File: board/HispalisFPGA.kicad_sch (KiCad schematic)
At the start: 111 parts, among them Q1 DMG1012T, Q2 DMG1012T, Q3 DMG1012T, Q4 DMG1012T, SW1 SW_DIP_x08

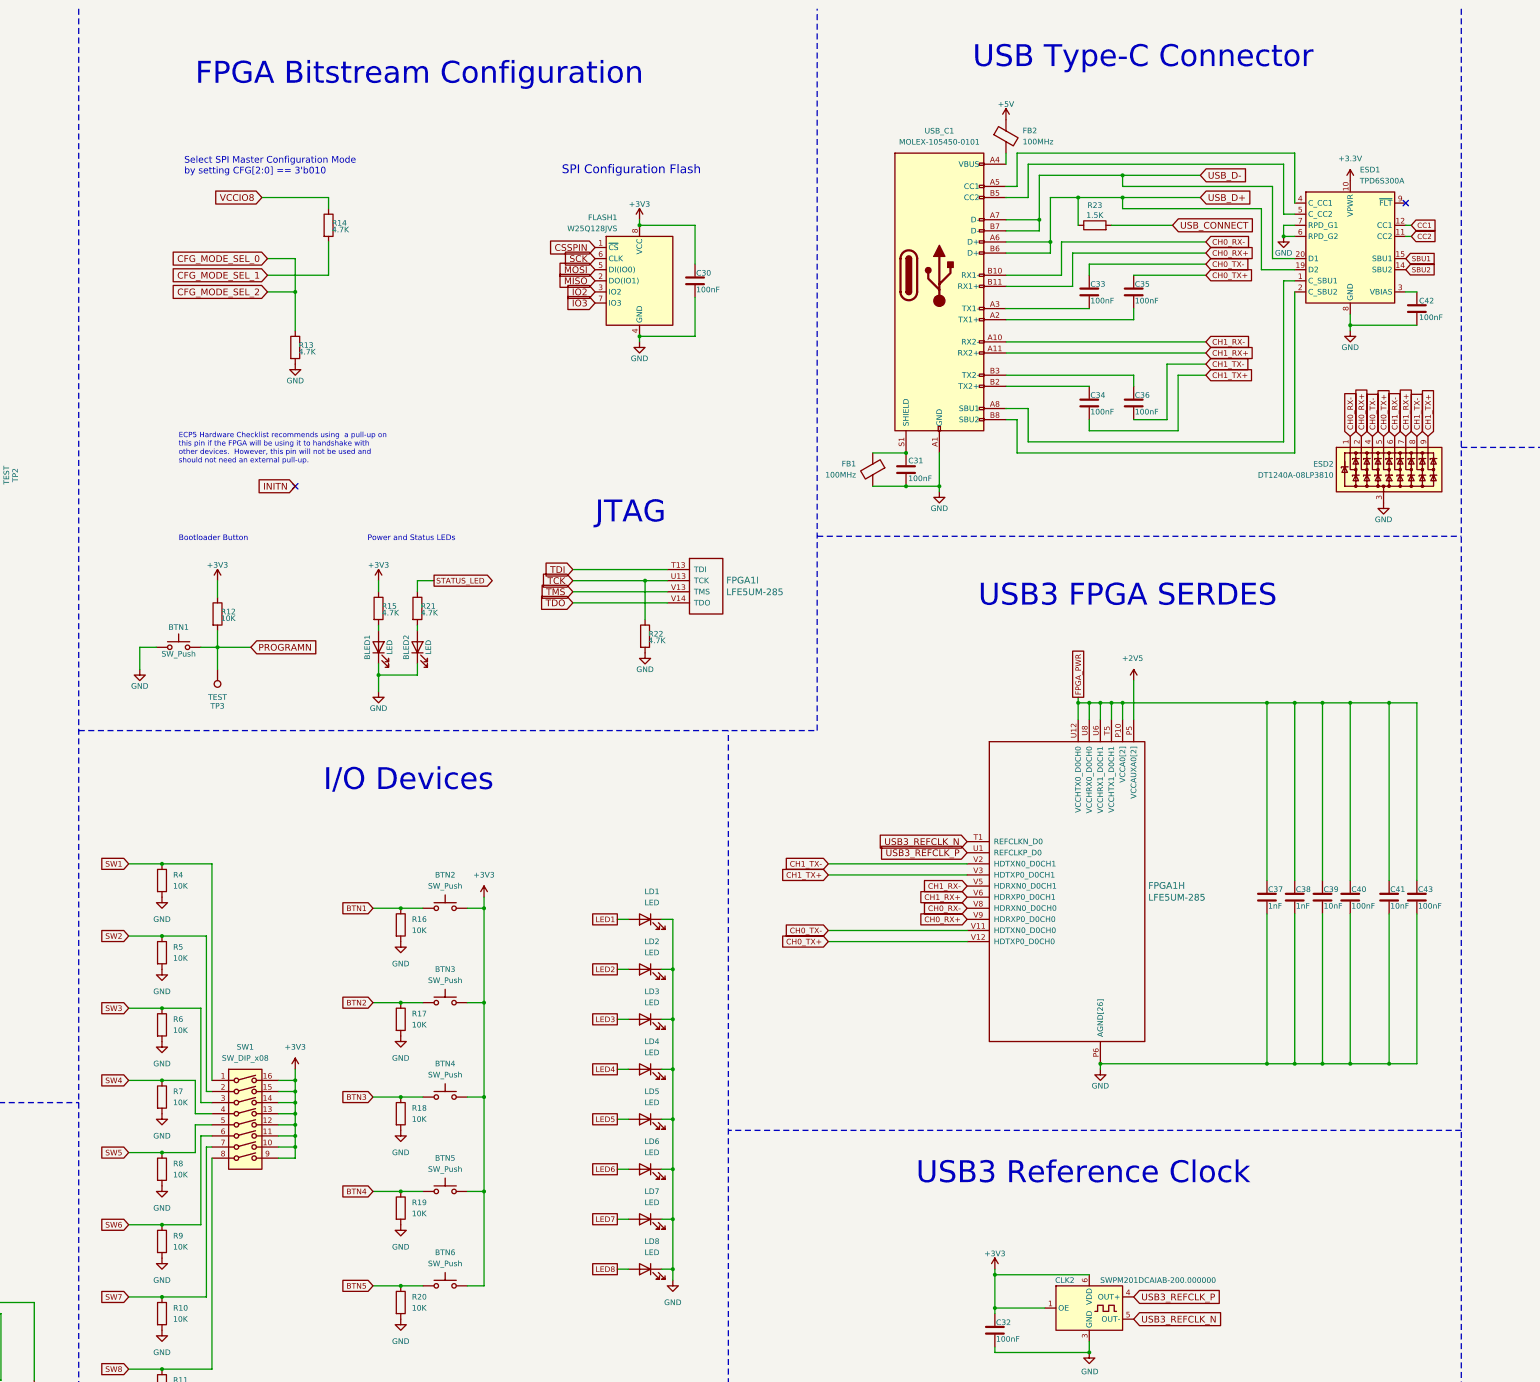
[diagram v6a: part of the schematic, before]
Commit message: Add missing ESD on 5V power line
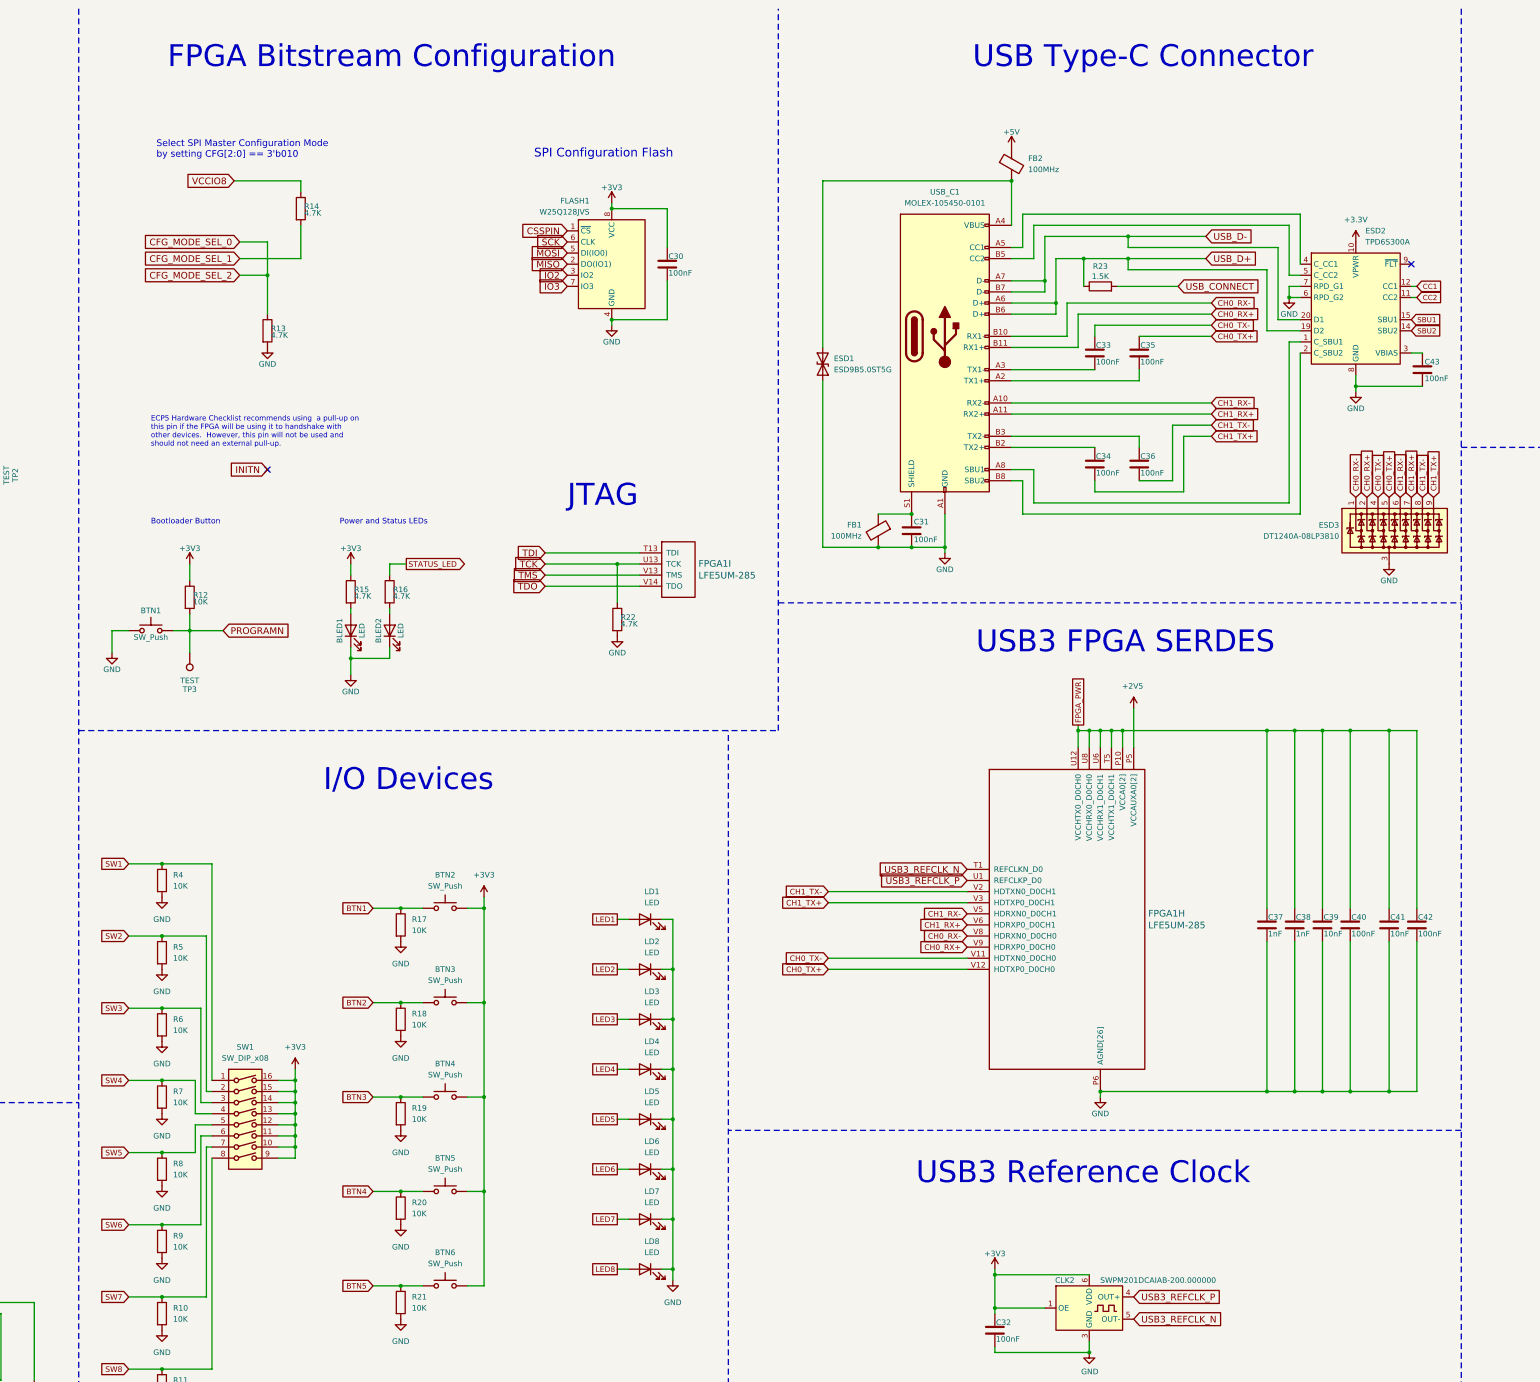
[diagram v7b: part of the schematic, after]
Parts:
- added ESD1: ESD9B5.0ST5G, Diode_SMD:D_SOD-923, symbol Diode:ESD9B5.0ST5G
- renumbered C43 to C42, C42 to C43, ESD1 to ESD2, ESD2 to ESD3, R21 to R16, R16 to R17, R17 to R18, R18 to R19, R19 to R20, R20 to R21
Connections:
- net GND: now also ESD1.1 (A1)
- net at FB2.2, USB_C1.A4 (VBUS), USB_C1.A9 (VBUS)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: now also ESD1.2 (A2)
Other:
- moved on the sheet: BLED1, BLED2, BTN1, C30, C31, C33, C34, C35, C36, C37, C38, C39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

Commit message: Final connection of ECP5 chip
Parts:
- removed C10, C17, C27: 100nF, Capacitor_SMD:C_0402_1005Metric, symbol Device:C
- removed C13, C19, C24, C28: 10nF, Capacitor_SMD:C_0402_1005Metric, symbol Device:C
- removed FPGA1: LFE5UM-285, Footprints:csfBGA 285, symbol HispalisFPGA:LFE5UM-285-Components
- added C20, C36: 100nF, Capacitor_SMD:C_0402_1005Metric, symbol Device:C
- added C21, C23, C43: 10nF, Capacitor_SMD:C_0402_1005Metric, symbol Device:C
- added C25, C26: 1nF, Capacitor_SMD:C_0402_1005Metric, symbol Device:C
- added FPGA1: LFE5UM-381, Package_BGA:Lattice_caBGA-381_17.0x17.0mm_Layout20x20_P0.8mm_Ball0.4mm_Pad0.4mm_NSMD, symbol FPGA_Lattice:LFE5UM-85F-6BG381x
- C37: value 1nF -> 10nF; LCSC C1523 -> C15195
- C38: value 1nF -> 100nF; LCSC C1523 -> C1525
- DISPLAY1: footprint Display_7Segment:CA56-12SRWA -> HispalisFPGA:MHDC3641SRBW
- PMOD1, PMOD2, PMOD3, PMOD4: footprint Connector_PinSocket_2.54mm:PinSocket_2x06_P2.54mm_Horizontal -> HispalisFPGA:PMOD_Socket_Horizontal
- renumbered BLED2 to BLED1, BLED1 to BLED2, BTN1 to BOOT_BTN1, BTN2 to BTN1, BTN3 to BTN2, BTN4 to BTN3, BTN5 to BTN4, BTN6 to BTN5, C7 to C1, C6 to C10, C9 to C11, C21 to C13, C23 to C16, C16 to C17, C25 to C18, C26 to C19, C11 to C2, C29 to C24, C30 to C27, C32 to C28, C31 to C29, C4 to C3, C33 to C30, C34 to C31, C35 to C32, C36 to C33, C43 to C34, C1 to C35, C18 to C4, C20 to C6, C8 to C7, C2 to C8, C3 to C9, CLK2 to CLK1, CLK1 to CLK2, 2V5_LDO_REG1 to LDO_REG1, R16 to R12, R15 to R13, R12 to R14, R17 to R15, R18 to R16, R19 to R17, R20 to R18, R21 to R19, R14 to R20, R13 to R21, 3V3_SW_REG1 to SW_REG1, 1V1_SW_REG1 to SW_REG2
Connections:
- net +3.3V is gone; now on net +3V3: ESD2.10 (VPWR)
- net +2V5: now also FPGA1.F15 (VCCAUX), FPGA1.F6 (VCCAUX), FPGA1.P15 (VCCAUX), FPGA1.P6 (VCCAUX), FPGA1.V10 (VCCAUXA0), FPGA1.V11 (VCCAUXA0), FPGA1.V17 (VCCAUXA1), FPGA1.V18 (VCCAUXA1)
- net +3V3: now also C37.1, C38.1, C39.1, C40.1, C41.1, C42.1, SW1.1, SW1.2, SW1.3, SW1.4, SW1.5, SW1.6, SW1.7, SW1.8, C36.1, C43.1, FPGA1.F10 (VCCIO0), FPGA1.F11 (VCCIO1), FPGA1.F12 (VCCIO1), FPGA1.F9 (VCCIO0), FPGA1.H14 (VCCIO2), FPGA1.H15 (VCCIO2), FPGA1.H6 (VCCIO7), FPGA1.H7 (VCCIO7), FPGA1.J15 (VCCIO2), FPGA1.J6 (VCCIO7), FPGA1.L14 (VCCIO3), FPGA1.L15 (VCCIO3), FPGA1.L6 (VCCIO6), FPGA1.L7 (VCCIO6), FPGA1.M15 (VCCIO3), FPGA1.M6 (VCCIO6), FPGA1.P10 (VCCIO8), FPGA1.P9 (VCCIO8); no longer C22.1, SW1.10, SW1.11, SW1.12, SW1.13, SW1.14, SW1.15, SW1.16, SW1.9
- net BTN1: now also FPGA1.F1 (PL47B)
- net BTN2: now also FPGA1.G1 (PL47D)
- net BTN3: now also FPGA1.H1 (PL53C)
- net BTN4: now also FPGA1.G2 (PL47A)
- net BTN5: now also FPGA1.F2 (PL44C)
- net CC1: now also FPGA1.U18 (PR92A)
- net CC2: now also FPGA1.U17 (PR92B)
- net CH0_RX+: now also FPGA1.Y5 (HDRXP0_D0CH0)
- net CH0_RX-: now also FPGA1.Y6 (HDRXN0_D0CH0)
- net CH0_TX+: now also FPGA1.W4 (HDTXP0_D0CH0)
- net CH0_TX-: now also FPGA1.W5 (HDTXN0_D0CH0)
- net CH1_RX+: now also FPGA1.Y7 (HDRXP0_D0CH1)
- net CH1_RX-: now also FPGA1.Y8 (HDRXN0_D0CH1)
- net CH1_TX+: now also FPGA1.W8 (HDTXP0_D0CH1)
- net CH1_TX-: now also FPGA1.W9 (HDTXN0_D0CH1)
- net CLK_16MHz: now also FPGA1.C20 (PR35A)
- net CSSPIN: now also FPGA1.R2 (PB15A)
- net GND: now also C20.2, C21.2, C23.2, C25.2, C26.2, C36.2, C43.2, FPGA1.B14 (GND), FPGA1.B7 (GND), FPGA1.C19 (GND), FPGA1.D4 (GND), FPGA1.F13 (GND), FPGA1.F14 (GND), FPGA1.F7 (GND), FPGA1.F8 (GND), FPGA1.G10 (GND), FPGA1.G11 (GND), FPGA1.G12 (GND), FPGA1.G13 (GND), FPGA1.G14 (GND), FPGA1.G15 (GND), FPGA1.G17 (GND), FPGA1.G4 (GND), FPGA1.G6 (GND), FPGA1.G7 (GND), FPGA1.G8 (GND), FPGA1.G9 (GND), FPGA1.H19 (GND), FPGA1.J10 (GND), FPGA1.J11 (GND), FPGA1.J12 (GND), FPGA1.J14 (GND), FPGA1.J2 (GND), FPGA1.J7 (GND), FPGA1.J9 (GND), FPGA1.K10 (GND), FPGA1.K11 (GND), FPGA1.K12 (GND), FPGA1.K14 (GND), FPGA1.K15 (GND), FPGA1.K6 (GND), FPGA1.K7 (GND), FPGA1.K9 (GND), FPGA1.L10 (GND), FPGA1.L11 (GND), FPGA1.L12 (GND), FPGA1.L9 (GND), FPGA1.M10 (GND), FPGA1.M11 (GND), FPGA1.M12 (GND), FPGA1.M14 (GND), FPGA1.M16 (GND), FPGA1.M2 (GND), FPGA1.M7 (GND), FPGA1.M9 (GND), FPGA1.N14 (GND), FPGA1.N15 (GND), FPGA1.N6 (GND), FPGA1.N7 (GND), FPGA1.P11 (GND), FPGA1.P12 (GND), FPGA1.P13 (GND), FPGA1.P14 (GND), FPGA1.P7 (GND), FPGA1.P8 (GND), FPGA1.R19 (GND), FPGA1.U10 (GND), FPGA1.U11 (GND), FPGA1.U12 (GND), FPGA1.U13 (GND), FPGA1.U14 (GND), FPGA1.U7 (GND), FPGA1.U8 (GND), FPGA1.U9 (GND), FPGA1.V12 (GND), FPGA1.V13 (GND), FPGA1.V14 (GND), FPGA1.V15 (GND), FPGA1.V16 (GND), FPGA1.V19 (GND), FPGA1.V20 (GND), FPGA1.V5 (GND), FPGA1.V6 (GND), FPGA1.V7 (GND), FPGA1.V8 (GND), FPGA1.V9 (GND), FPGA1.W12 (GND), FPGA1.W15 (GND), FPGA1.W16 (GND), FPGA1.W19 (GND), FPGA1.W6 (GND), FPGA1.W7 (GND)
- net IO2: now also FPGA1.Y2 (PB9B)
- net IO3: now also FPGA1.W1 (PB9A)
- net LED1: now also FPGA1.A13 (PT76B)
- net LED2: now also FPGA1.B13 (PT78A)
- net LED3: now also FPGA1.A12 (PT76A)
- net LED4: now also FPGA1.B12 (PT71A)
- net LED5: now also FPGA1.A11 (PT63B)
- net LED6: now also FPGA1.B11 (PT65A)
- net LED7: now also FPGA1.A10 (PT63A)
- net LED8: now also FPGA1.B10 (PT60B)
- net MISO: now also FPGA1.V2 (PB11A)
- net MOSI: now also FPGA1.W2 (PB11B)
- net PMOD1_1: now also FPGA1.L19 (PR47C)
- net PMOD1_10: now also FPGA1.P20 (PR86A)
- net PMOD1_2: now also FPGA1.M19 (PR47D)
- net PMOD1_3: now also FPGA1.N19 (PR83A)
- net PMOD1_4: now also FPGA1.P19 (PR83C)
- net PMOD1_7: now also FPGA1.L20 (PR47A)
- net PMOD1_8: now also FPGA1.M20 (PR47B)
- net PMOD1_9: now also FPGA1.N20 (PR83B)
- net PMOD2_1: now also FPGA1.D19 (PR35B)
- net PMOD2_10: now also FPGA1.G20 (PR38D)
- net PMOD2_2: now also FPGA1.E19 (PR35D)
- net PMOD2_3: now also FPGA1.F19 (PR38B)
- net PMOD2_4: now also FPGA1.G19 (PR41A)
- net PMOD2_7: now also FPGA1.D20 (PR35C)
- net PMOD2_8: now also FPGA1.E20 (PR38A)
- net PMOD2_9: now also FPGA1.F20 (PR38C)
- net PMOD3_1: now also FPGA1.P2 (PL92B)
- net PMOD3_10: now also FPGA1.K1 (PL53D)
- net PMOD3_2: now also FPGA1.N2 (PL89A)
- net PMOD3_3: now also FPGA1.L2 (PL86D)
- net PMOD3_4: now also FPGA1.K2 (PL53A)
- net PMOD3_7: now also FPGA1.P1 (PL92A)
- net PMOD3_8: now also FPGA1.N1 (PL89D)
- net PMOD3_9: now also FPGA1.L1 (PL89C)
- net PMOD4_1: now also FPGA1.E2 (PL44D)
- net PMOD4_10: now also FPGA1.B1 (PL35B)
- net PMOD4_2: now also FPGA1.D2 (PL38C)
- net PMOD4_3: now also FPGA1.C2 (PL35D)
- net PMOD4_4: now also FPGA1.B2 (PL35C)
- net PMOD4_7: now also FPGA1.E1 (PL38D)
- net PMOD4_8: now also FPGA1.D1 (PL38B)
- net PMOD4_9: now also FPGA1.C1 (PL38A)
- net PROGRAMN: now also FPGA1.T20 (PR86C), FPGA1.W3 (~{PROGRAM})
- net SBU1: now also FPGA1.U20 (PR86D)
- net SBU2: now also FPGA1.U19 (PR89C)
- net SCK: now also FPGA1.U3 (CCLK)
- net SW1: now also SW1.16, FPGA1.A6 (PT4A); no longer SW1.1
- net SW2: now also SW1.15, FPGA1.B6 (PT4B); no longer SW1.2
- net SW3: now also SW1.14, FPGA1.A5 (PL11B); no longer SW1.3
- net SW4: now also SW1.13, FPGA1.B5 (PL11C); no longer SW1.4
- net SW5: now also SW1.12, FPGA1.A4 (PL11A); no longer SW1.5
- net SW6: now also SW1.11, FPGA1.B4 (PL14B); no longer SW1.6
- net SW7: now also SW1.10, FPGA1.A3 (PL14C); no longer SW1.7
- net SW8: now also SW1.9, FPGA1.B3 (PL14D); no longer SW1.8
- net TCK: now also FPGA1.T5 (TCK)
- net TDI: now also FPGA1.R5 (TDI)
- net TDO: now also FPGA1.V4 (TDO)
- net TMS: now also FPGA1.U5 (TMS)
- net USB_CONNECT: now also FPGA1.P5 (PL83D)
- net USB_D+: now also FPGA1.N3 (PL86A)
- net USB_D-: now also FPGA1.M3 (PL86B)
- net CFG_MODE_SEL_0: no longer names the net of R21.1
- net CFG_MODE_SEL_0: now also FPGA1.R4 (CFG_2), FPGA1.U4 (CFG_0)
- net CFG_MODE_SEL_1: no longer names the net of R20.2
- net CFG_MODE_SEL_1: now also FPGA1.T4 (CFG_1)
- net DISPLAY_A1 renamed DISPLAY_D1
- net DISPLAY_D1: now also FPGA1.A19 (PT121A)
- net DISPLAY_A2 renamed DISPLAY_D2
- net DISPLAY_D2: now also FPGA1.A16 (PT110A)
- net DISPLAY_A3 renamed DISPLAY_D3
- net DISPLAY_D3: now also FPGA1.A15 (PT103A)
- net DISPLAY_A4 renamed DISPLAY_D4
- net DISPLAY_D4: now also FPGA1.B15 (PT105A)
- net DISPLAY_CA renamed DISPLAY_SA
- net DISPLAY_SA: now also FPGA1.A18 (PT119A)
- net DISPLAY_CB renamed DISPLAY_SB
- net DISPLAY_SB: now also FPGA1.A14 (PT83A)
- net DISPLAY_CC renamed DISPLAY_SC
- net DISPLAY_SC: now also FPGA1.B17 (PT114A)
- net DISPLAY_CD renamed DISPLAY_SD
- net DISPLAY_SD: now also FPGA1.B19 (PT119B)
- net DISPLAY_CDP renamed DISPLAY_SDP
- net DISPLAY_SDP: now also FPGA1.B18 (PT116B)
- net DISPLAY_CE renamed DISPLAY_SE
- net DISPLAY_SE: now also FPGA1.B20 (PT121B)
- net DISPLAY_CF renamed DISPLAY_SF
- net DISPLAY_SF: now also FPGA1.A17 (PT116A)
- net DISPLAY_CG renamed DISPLAY_SG
- net DISPLAY_SG: now also FPGA1.B16 (PT110B)
- net FPGA_PWR renamed +1V1
- net +1V1: now also C22.1, C20.1, C21.1, C23.1, C25.1, C26.1, FPGA1.H10 (VCC), FPGA1.H11 (VCC), FPGA1.H12 (VCC), FPGA1.H13 (VCC), FPGA1.H8 (VCC), FPGA1.H9 (VCC), FPGA1.J13 (VCC), FPGA1.J8 (VCC), FPGA1.K13 (VCC), FPGA1.K8 (VCC), FPGA1.L13 (VCC), FPGA1.L8 (VCC), FPGA1.M13 (VCC), FPGA1.M8 (VCC), FPGA1.N10 (VCC), FPGA1.N11 (VCC), FPGA1.N12 (VCC), FPGA1.N13 (VCC), FPGA1.N8 (VCC), FPGA1.N9 (VCC), FPGA1.T10 (VCCHTX1_D0CH1), FPGA1.T11 (VCCHTX0_D1CH0), FPGA1.T12 (VCCHRX0_D1CH0), FPGA1.T13 (VCCHRX1_D1CH1), FPGA1.T14 (VCCHTX1_D1CH1), FPGA1.T15 (VCCA1), FPGA1.T6 (VCCA0), FPGA1.T7 (VCCHTX0_D0CH0), FPGA1.T8 (VCCHRX0_D0CH0), FPGA1.T9 (VCCHRX1_D0CH1), FPGA1.U15 (VCCA1), FPGA1.U6 (VCCA0); no longer C37.1, C38.1, C39.1, C40.1, C41.1, C42.1
- net STATUS_LED: no longer names the net of R12.1
- net STATUS_LED: now also FPGA1.Y3 (DONE)
- net USB3_REFCLK_N: no longer names the net of CLK1.5 (OUT-)
- net USB3_REFCLK_N: now also FPGA1.Y12 (REFCLKN_D0)
- net USB3_REFCLK_P: no longer names the net of CLK1.4 (OUT+)
- net USB3_REFCLK_P: now also FPGA1.Y11 (REFCLKP_D0)
- no-connect marks 2 -> 138
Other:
- note added: "ECP5 Hardware Checklist recommends using a pull-up on the pin INIT if the FPGA will be using it to handshake with other devices. However, this pin will not be used and should not need an external pull-up."
- note added: "PMOD Connectors"
- note added: "Status and Power LEDs"
- note removed: "Board Connectors"
- note removed: "ECP5 Hardware Checklist recommends using a pull-up on this pin if the FPGA will be using it to handshake with other devices. However, this pin will not be used and should not need an external pull-up."
- note removed: "JTAG"
- note removed: "Power and Status LEDs"
- note removed: "USB3 Reference Clock"
- moved on the sheet: 5V_LINE1, BLED1, BLED2, BOOT_BTN1, BTN1, BTN2, BTN3, BTN4, BTN5, C1, C10, C11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
